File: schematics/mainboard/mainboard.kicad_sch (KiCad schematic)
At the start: 28 parts, among them J1 ICSP, J2 USB_B_Micro, J3 DEALON DC-S050-200, J4 PWR_SELECT, J5 JOY1, U1 ATmega2560-16A, U2 FT232RL, U3 USBLC6-2P6, U4 AIP78M05, Y1 16Mhz

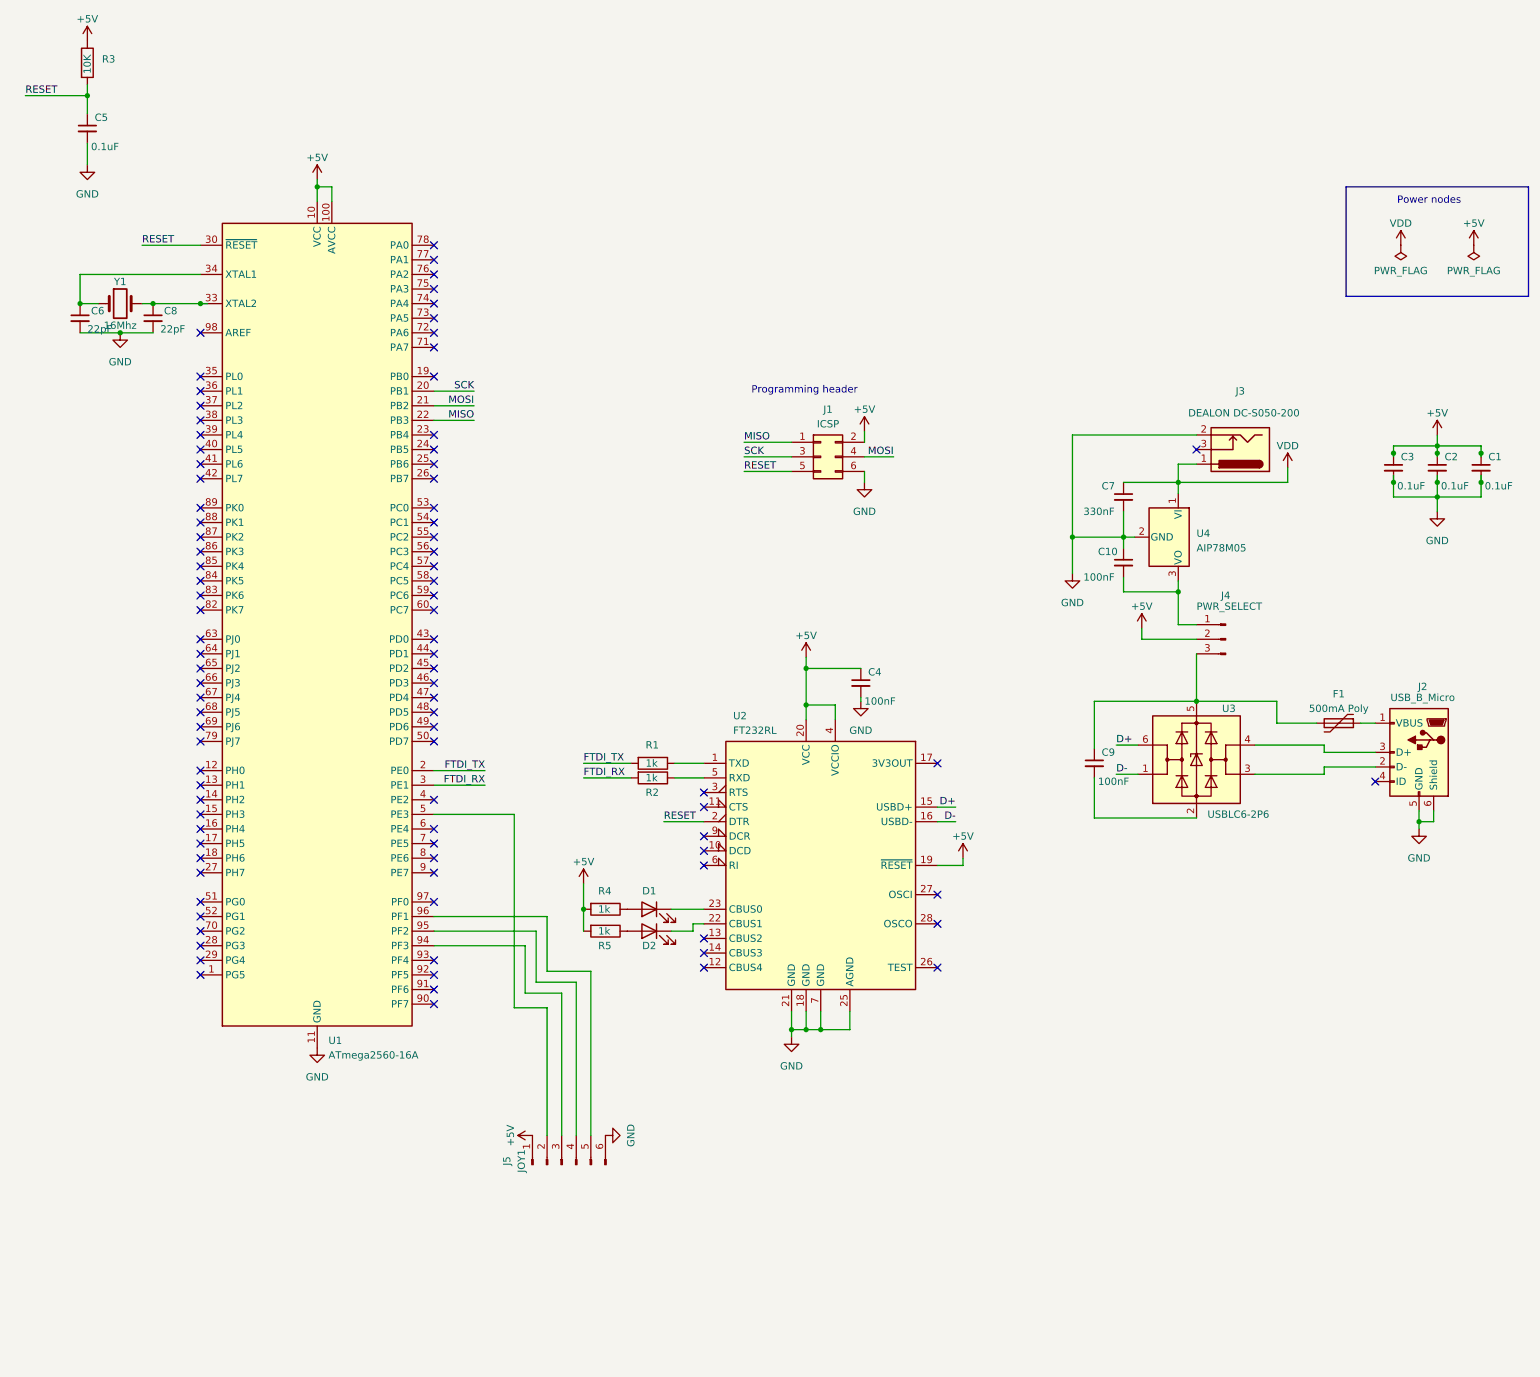
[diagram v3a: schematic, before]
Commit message: SCH: mainboard=> joy2 header + throttle header
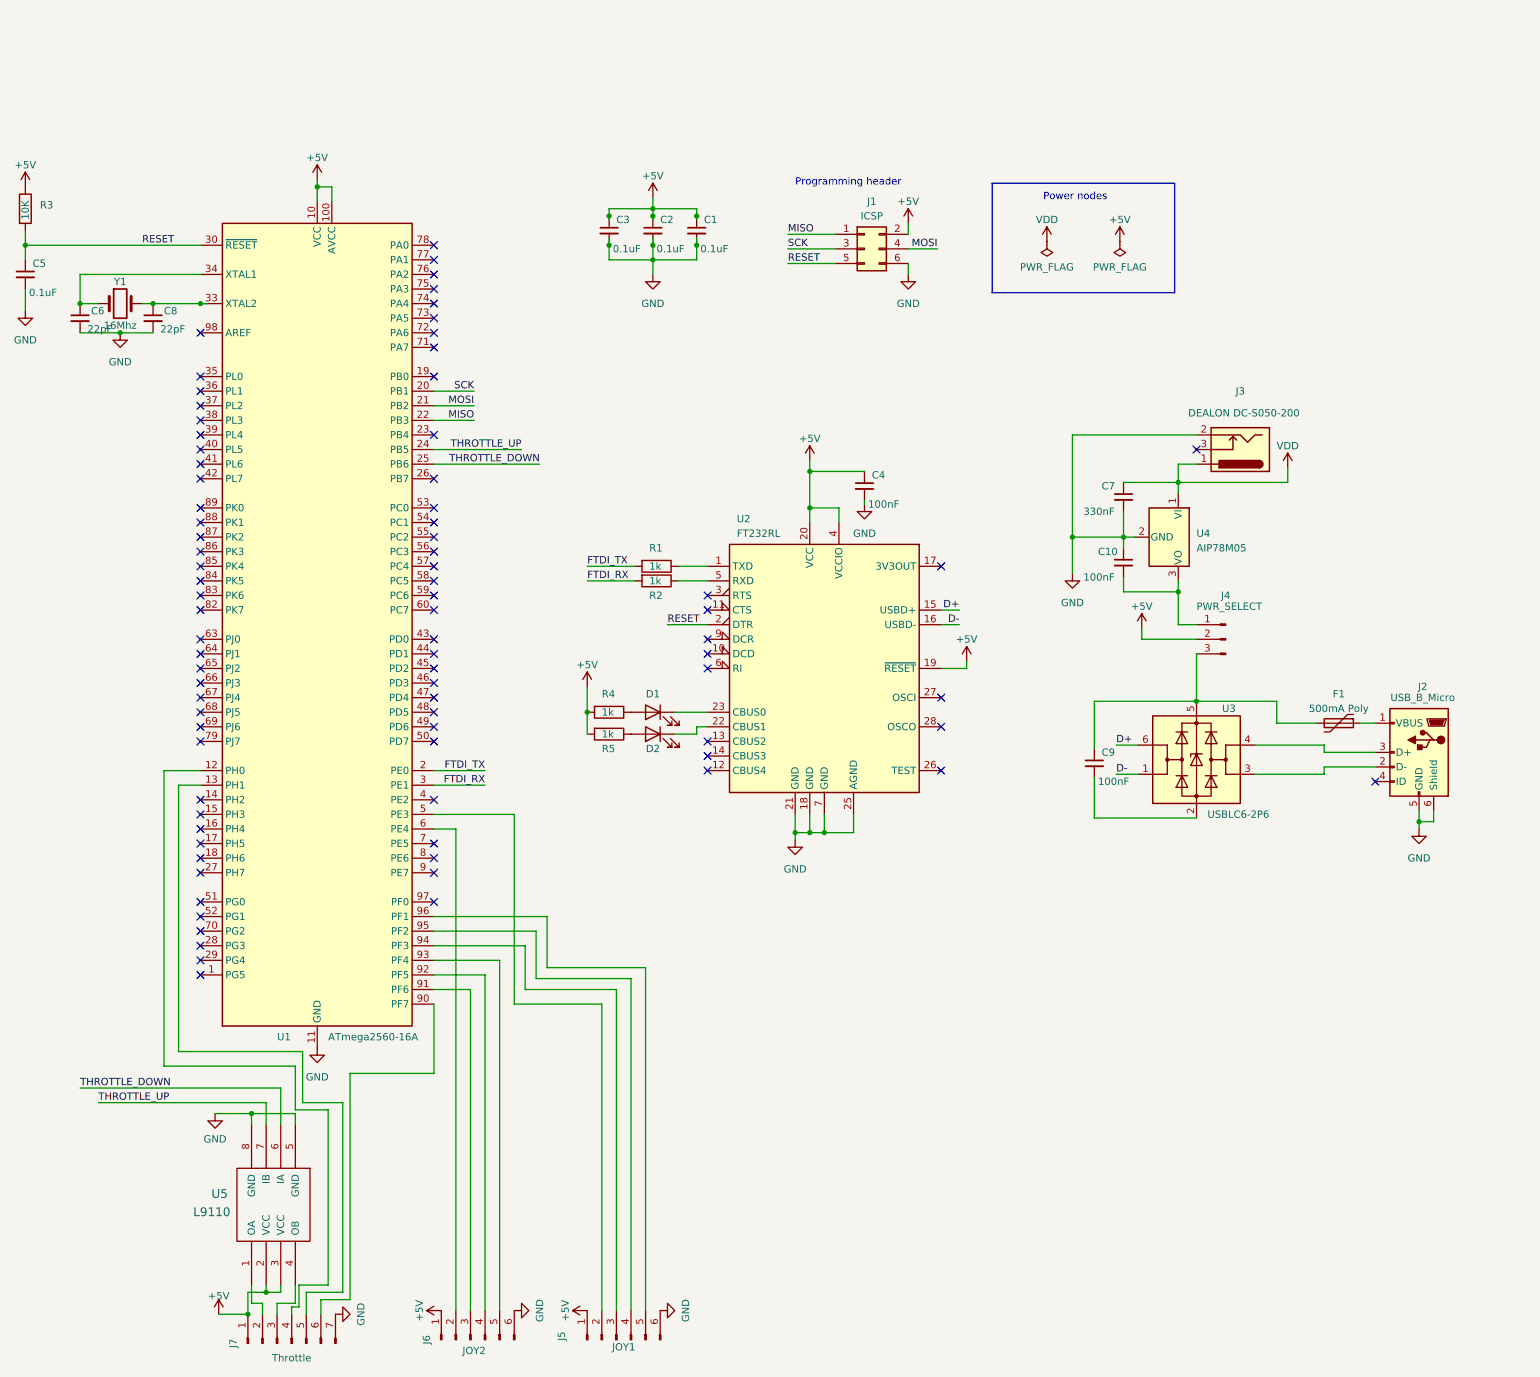
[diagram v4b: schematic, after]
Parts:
- added J6: JOY2, Connector_JST:JST_PH_B6B-PH-K_1x06_P2.00mm_Vertical, symbol Connector:Conn_01x06_Pin
- added J7: Throttle, Connector_JST:JST_PH_B7B-PH-K_1x07_P2.00mm_Vertical, symbol Connector:Conn_01x07_Pin
- added U5: L9110, Package_SO:SOP-8_3.9x4.9mm_P1.27mm, symbol l9110_lib:L9110
- C1, C2, C3, C4, C5, C9: footprint Capacitor_SMD:C_0201_0603Metric -> Capacitor_SMD:C_0603_1608Metric
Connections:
- net +5V: now also J6.1 (Pin_1), J7.1 (Pin_1), U5.2 (VCC), U5.3 (VCC)
- net GND: now also J6.6 (Pin_6), J7.7 (Pin_7), U5.5 (GND), U5.8 (GND)
- net at U1.12 (PH0): now also J7.4 (Pin_4)
- net at U1.13 (PH1): now also J7.5 (Pin_5)
- net THROTTLE_UP: now reaches U1.24 (PB5)
- net THROTTLE_UP: now also U5.7 (IB)
- net THROTTLE_DOWN: now reaches U1.25 (PB6)
- net THROTTLE_DOWN: now also U5.6 (IA)
- net at U1.6 (PE4): now also J6.2 (Pin_2)
- net at U1.90 (PF7): now also J7.6 (Pin_6)
- net at U1.91 (PF6): now also J6.3 (Pin_3)
- net at U1.92 (PF5): now also J6.4 (Pin_4)
- net at U1.93 (PF4): now also J6.5 (Pin_5)
- new net: J7.2 (Pin_2), U5.1 (OA)
- new net: J7.3 (Pin_3), U5.4 (OB)
- no-connect marks 92 -> 83
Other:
- moved on the sheet: C1, C2, C3, C4, C5, D1, D2, J1, J5, R1, R2, R3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

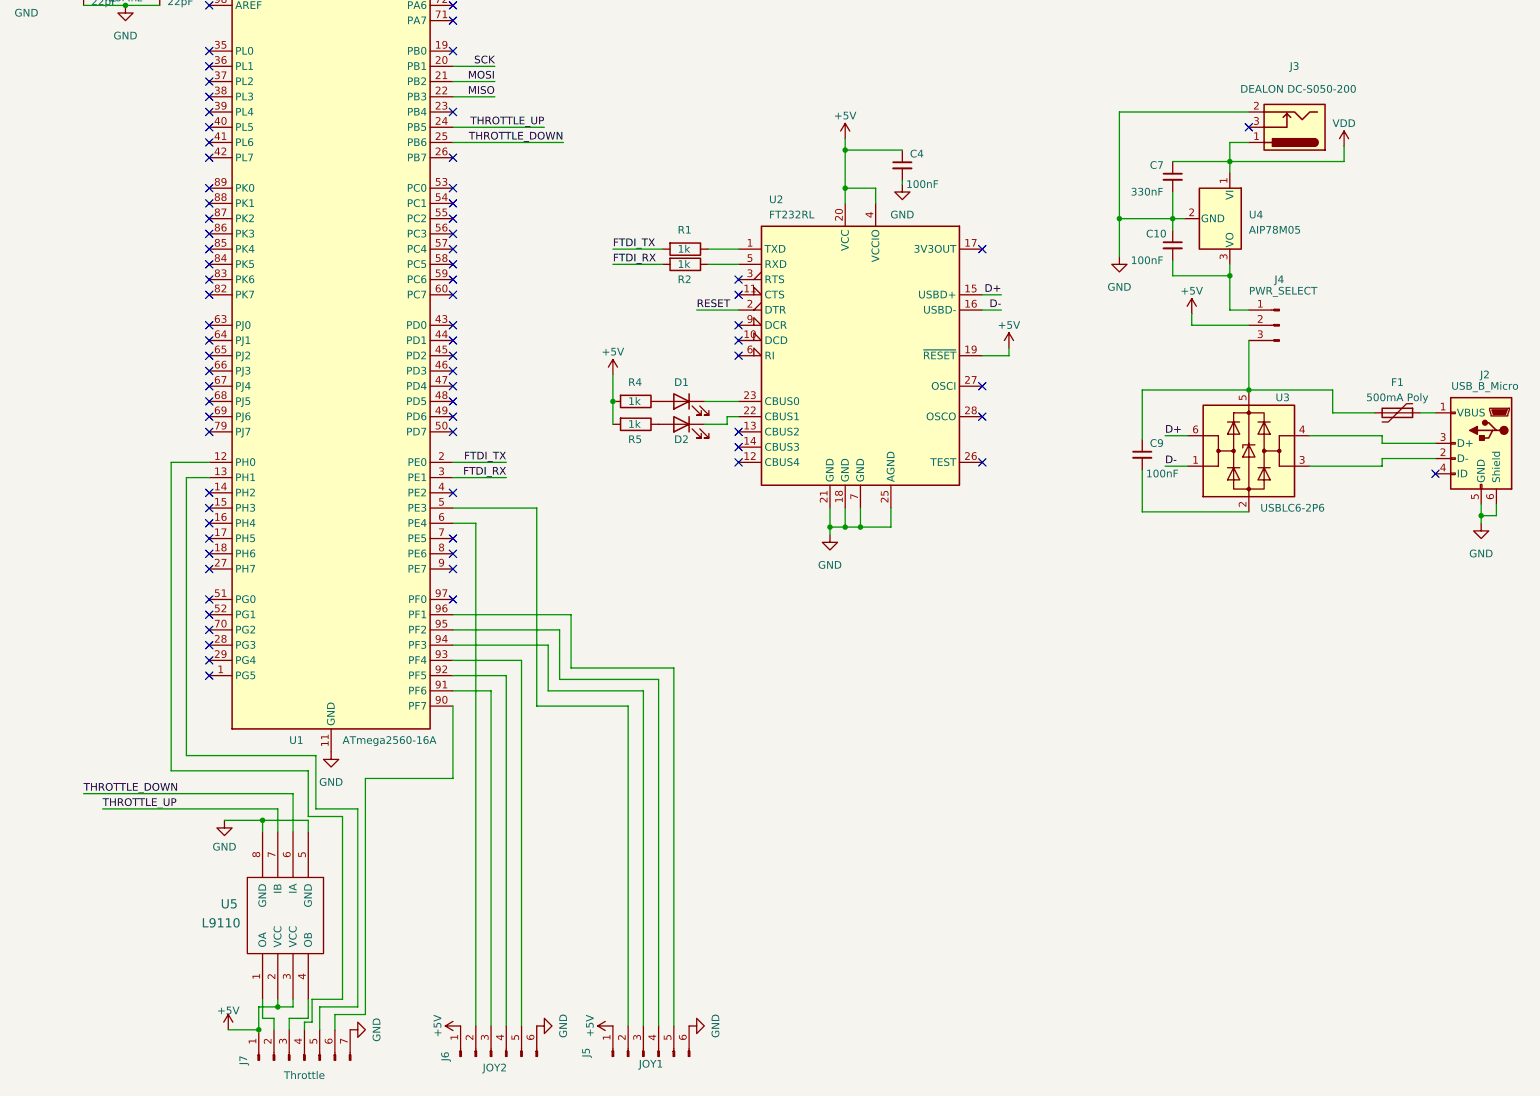
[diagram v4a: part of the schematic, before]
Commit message: SCH: mainboard=> DGAUGES header
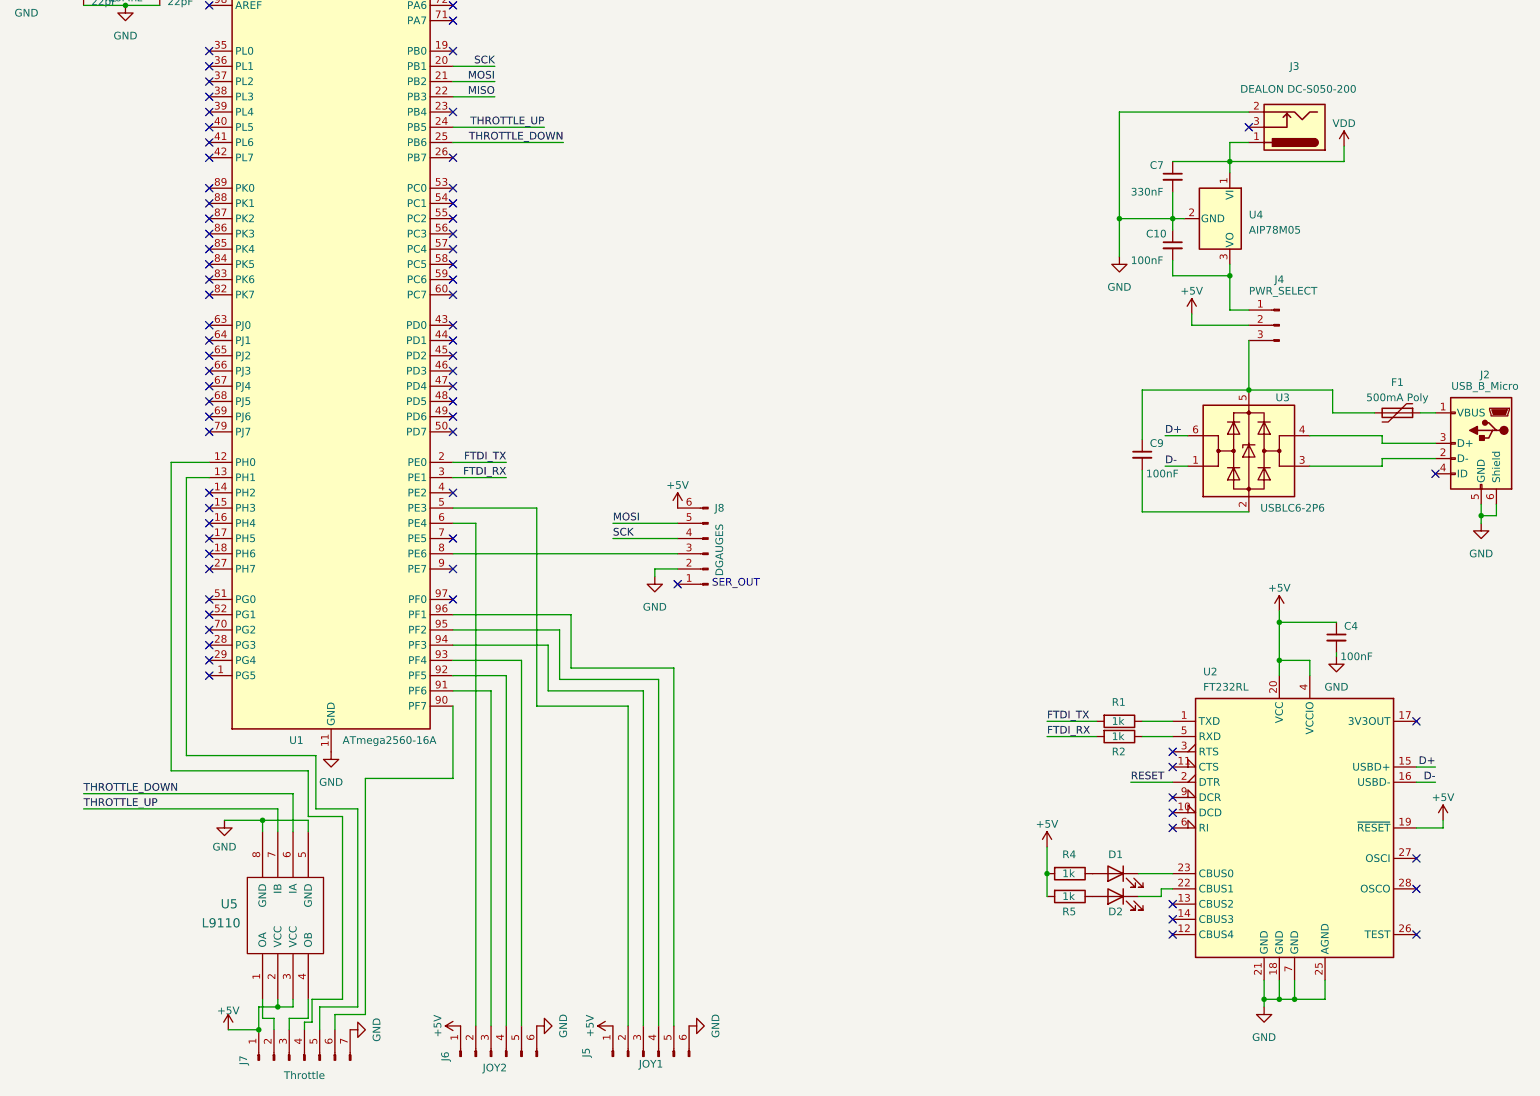
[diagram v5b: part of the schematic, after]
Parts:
- added J8: DGAUGES, Connector_JST:JST_PH_B6B-PH-K_1x06_P2.00mm_Vertical, symbol Connector:Conn_01x06_Pin
- U5: footprint Package_SO:SOP-8_3.9x4.9mm_P1.27mm -> Package_DIP:DIP-8_W7.62mm_Socket
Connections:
- net +5V: now also J8.6 (Pin_6)
- net GND: now also J8.2 (Pin_2)
- net MOSI: now also J8.5 (Pin_5)
- net SCK: now also J8.4 (Pin_4)
- net at U1.8 (PE6): now also J8.3 (Pin_3)
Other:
- note added: "SER_OUT"
- moved on the sheet: C4, D1, D2, R1, R2, R4, R5, U2
